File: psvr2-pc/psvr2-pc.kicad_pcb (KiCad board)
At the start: 2 copper layers, 5 parts, among them Q1 IRLML6244, U1 RP2040, U2 M95256-WMN6P, U3 FUSB302B01MPX, U4 FUSB302B01MPX

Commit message: Mess around with KiBuzzard and the PCB Editor.
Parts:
- added kibuzzard-65BD64CF: G***, kibuzzard-65BD64CF, F.Cu at (63.5, 22.9)
- moved U3 89.8 mm to (126.2, 26.7)
- moved U4 32.1 mm to (67.3, 50.3)
- moved U1 29.1 mm to (58.4, 37.2)
- moved U2 10.3 mm to (20.3, 38.7)
- moved Q1 4.74 mm to (42.2, 24.4)

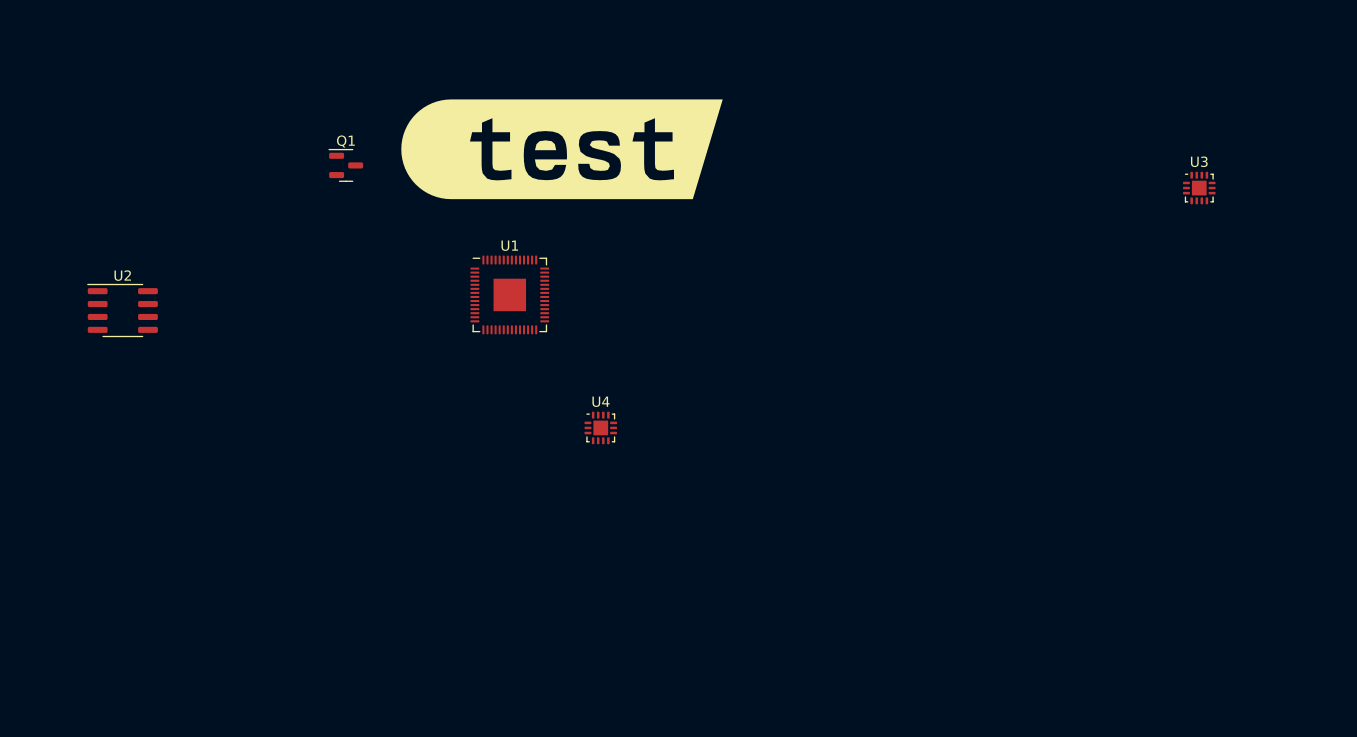
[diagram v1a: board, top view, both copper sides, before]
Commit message: Start documenting the valid half-duplex M-LVDS transceivers >1Mbps that work for converting the differential DP-AUX signals into something that the microcontroller GPIO can understand.
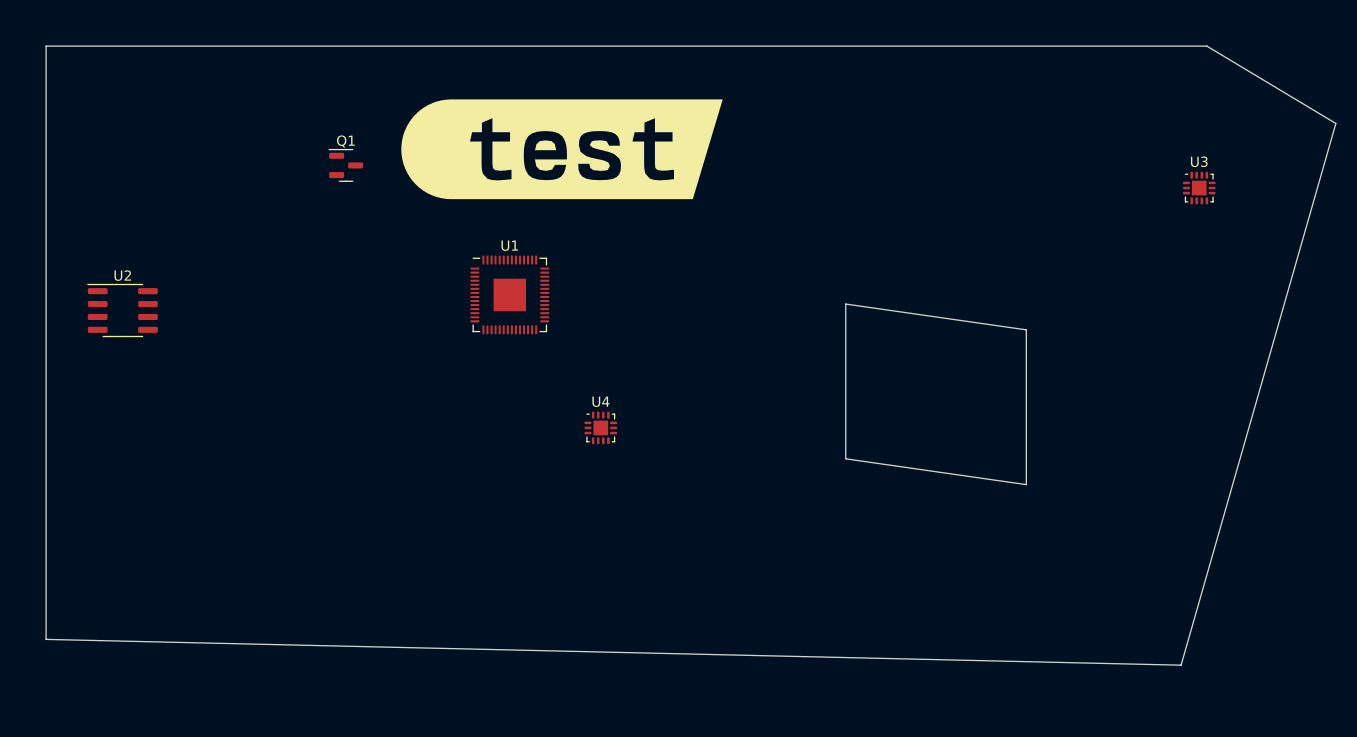
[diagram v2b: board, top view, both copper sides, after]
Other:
- board outline added: 127 x 61 mm
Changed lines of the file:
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@@
     (attr board_only exclude_from_pos_files exclude_from_bom)
     (fp_text reference "kibuzzard-65BD64CF" (at 0 -7.958243) (layer "F.SilkS") hide
-        (effects (font (size 0 0)))
+        (effects (font (size 0 0) (thickness 0.15)))
     )
     (fp_text value "G***" (at 0 7.958243) (layer "F.SilkS") hide
-        (effects (font (size 0 0)))
+        (effects (font (size 0 0) (thickness 0.15)))
     )
     (fp_poly
@@
       (stroke (width 0) (type solid)) (fill solid) (layer "F.SilkS"))
   )
+  (gr_line (start 109.22 55.88) (end 109.22 40.64)
+    (stroke (width 0.1) (type default)) (layer "Edge.Cuts"))
+  (gr_line (start 91.44 38.1) (end 91.44 53.34)
+    (stroke (width 0.1) (type default)) (layer "Edge.Cuts"))
+  (gr_line (start 139.7 20.32) (end 127 12.7)
+    (stroke (width 0.1) (type default)) (layer "Edge.Cuts"))
+  (gr_line (start 109.22 40.64) (end 91.44 38.1)
+    (stroke (width 0.1) (type default)) (layer "Edge.Cuts"))
+  (gr_line (start 124.46 73.66) (end 139.7 20.32)
+    (stroke (width 0.1) (type default)) (layer "Edge.Cuts"))
+  (gr_line (start 12.7 12.7) (end 12.7 71.12)
+    (stroke (width 0.1) (type default)) (layer "Edge.Cuts"))
+  (gr_line (start 127 12.7) (end 12.7 12.7)
+    (stroke (width 0.1) (type default)) (layer "Edge.Cuts"))
+  (gr_line (start 12.7 71.12) (end 124.46 73.66)
+    (stroke (width 0.1) (type default)) (layer "Edge.Cuts"))
+  (gr_line (start 91.44 53.34) (end 109.22 55.88)
+    (stroke (width 0.1) (type default)) (layer "Edge.Cuts"))
 )

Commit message: Mark the power and config DisplayPort pins as not connected.
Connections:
- U1 pad 2: unconnected-(U1-GPIO0-Pad2) -> /HMD_TYC_SDA
- U1 pad 3: unconnected-(U1-GPIO1-Pad3) -> /HMD_TYC_SCL
- U1 pad 4: unconnected-(U1-GPIO2-Pad4) -> /HMD_TYC_INT
- U1 pad 46: unconnected-(U1-USB_DM-Pad46) -> /PC_USB2.0_P
- U1 pad 47: unconnected-(U1-USB_DP-Pad47) -> /PC_USB2.0_N
- U1 pad 57: unconnected-(U1-GND-Pad57) -> GND
- U3 pad 2: unconnected-(U3-VBUS-Pad2) -> Net-(U3-VBUS)
- U3 pad 5: unconnected-(U3-INT_N-Pad5) -> /HMD_TYC_INT
- U3 pad 6: unconnected-(U3-SCL-Pad6) -> /HMD_TYC_SCL
- U3 pad 7: unconnected-(U3-SDA-Pad7) -> /HMD_TYC_SDA
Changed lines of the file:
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@@
   (net 3 "unconnected-(Q1-D-Pad3)")
   (net 4 "Net-(U1-IOVDD-Pad1)")
-  (net 5 "unconnected-(U1-GPIO0-Pad2)")
-  (net 6 "unconnected-(U1-GPIO1-Pad3)")
-  (net 7 "unconnected-(U1-GPIO2-Pad4)")
+  (net 5 "/HMD_TYC_SDA")
+  (net 6 "/HMD_TYC_SCL")
+  (net 7 "/HMD_TYC_INT")
   (net 8 "unconnected-(U1-GPIO3-Pad5)")
   (net 9 "unconnected-(U1-GPIO4-Pad6)")
@@
   (net 59 "unconnected-(U2-VCC-Pad8)")
   (net 60 "Net-(U3-VDD-Pad3)")
-  (net 61 "unconnected-(U3-INT_N-Pad5)")
-  (net 62 "unconnected-(U3-SCL-Pad6)")
-  (net 63 "unconnected-(U3-SDA-Pad7)")
+  (net 61 "/PC_USB2.0_P")
+  (net 62 "/PC_USB2.0_N")
+  (net 63 "GND")
   (net 64 "Net-(U3-GND-Pad15)")
   (net 65 "unconnected-(U3-VCONN-Pad12)")
@@
   (net 74 "unconnected-(U4-VCONN-Pad12)")
   (net 75 "unconnected-(U4-VCONN-Pad13)")
-  (net 76 "unconnected-(U3-VBUS-Pad2)")
-  (net 77 "unconnected-(U1-USB_DP-Pad47)")
-  (net 78 "unconnected-(U1-USB_DM-Pad46)")
-  (net 79 "unconnected-(U1-GND-Pad57)")
-  (net 80 "Net-(U4-CC2-Pad1)")
-  (net 81 "Net-(U3-CC2-Pad1)")
-  (net 82 "Net-(U3-CC1-Pad10)")
+  (net 76 "Net-(P1-VCONN)")
+  (net 77 "Net-(U3-VBUS)")
+  (net 78 "Net-(P1-CC)")
+  (net 79 "Net-(D2-K)")
   (footprint "Package_DFN_QFN:QFN-56-1EP_7x7mm_P0.4mm_EP3.2x3.2mm" (layer "F.Cu")
     (at 58.36 37.2025)
@@
       (net 4 "Net-(U1-IOVDD-Pad1)") (pinfunction "IOVDD") (pintype "power_in"))
     (pad "2" smd roundrect (at -3.4375 -2.2) (size 0.875 0.2) (layers "F.Cu" "F.Paste" "F.Mask") (roundrect_rratio 0.25)
-      (net 5 "unconnected-(U1-GPIO0-Pad2)") (pinfunction "GPIO0") (pintype "bidirectional"))
+      (net 5 "/HMD_TYC_SDA") (pinfunction "GPIO0") (pintype "bidirectional"))
     (pad "3" smd roundrect (at -3.4375 -1.8) (size 0.875 0.2) (layers "F.Cu" "F.Paste" "F.Mask") (roundrect_rratio 0.25)
-      (net 6 "unconnected-(U1-GPIO1-Pad3)") (pinfunction "GPIO1") (pintype "bidirectional"))
+      (net 6 "/HMD_TYC_SCL") (pinfunction "GPIO1") (pintype "bidirectional"))
     (pad "4" smd roundrect (at -3.4375 -1.4) (size 0.875 0.2) (layers "F.Cu" "F.Paste" "F.Mask") (roundrect_rratio 0.25)
-      (net 7 "unconnected-(U1-GPIO2-Pad4)") (pinfunction "GPIO2") (pintype "bidirectional"))
+      (net 7 "/HMD_TYC_INT") (pinfunction "GPIO2") (pintype "bidirectional"))
     (pad "5" smd roundrect (at -3.4375 -1) (size 0.875 0.2) (layers "F.Cu" "F.Paste" "F.Mask") (roundrect_rratio 0.25)
       (net 8 "unconnected-(U1-GPIO3-Pad5)") (pinfunction "GPIO3") (pintype "bidirectional"))
@@
       (net 44 "unconnected-(U1-VREG_VOUT-Pad45)") (pinfunction "VREG_VOUT") (pintype "power_out"))
     (pad "46" smd roundrect (at 1.4 -3.4375) (size 0.2 0.875) (layers "F.Cu" "F.Paste" "F.Mask") (roundrect_rratio 0.25)
-      (net 78 "unconnected-(U1-USB_DM-Pad46)") (pinfunction "USB_DM") (pintype "bidirectional"))
+      (net 61 "/PC_USB2.0_P") (pinfunction "USB_DM") (pintype "bidirectional"))
     (pad "47" smd roundrect (at 1 -3.4375) (size 0.2 0.875) (layers "F.Cu" "F.Paste" "F.Mask") (roundrect_rratio 0.25)
-      (net 77 "unconnected-(U1-USB_DP-Pad47)") (pinfunction "USB_DP") (pintype "bidirectional"))
+      (net 62 "/PC_USB2.0_N") (pinfunction "USB_DP") (pintype "bidirectional"))
     (pad "48" smd roundrect (at 0.6 -3.4375) (size 0.2 0.875) (layers "F.Cu" "F.Paste" "F.Mask") (roundrect_rratio 0.25)
       (net 45 "unconnected-(U1-USB_VDD-Pad48)") (pinfunction "USB_VDD") (pintype "power_in"))
@@
       (net 51 "unconnected-(U1-QSPI_SS-Pad56)") (pinfunction "QSPI_SS") (pintype "bidirectional"))
     (pad "57" smd rect (at 0 0) (size 3.2 3.2) (layers "F.Cu" "F.Mask")
-      (net 79 "unconnected-(U1-GND-Pad57)") (pinfunction "GND") (pintype "power_in"))
+      (net 63 "GND") (pinfunction "GND") (pintype "power_in"))
     (model "${KICAD6_3DMODEL_DIR}/Package_DFN_QFN.3dshapes/QFN-56-1EP_7x7mm_P0.4mm_EP3.2x3.2mm.wrl"
       (offset (xyz 0 0 0))
@@
     (pad "" smd roundrect (at 0.36 0.36) (size 0.58 0.58) (layers "F.Paste") (roundrect_rratio 0.25))
     (pad "1" smd roundrect (at -1.2625 -0.5) (size 0.675 0.25) (layers "F.Cu" "F.Paste" "F.Mask") (roundrect_rratio 0.25)
-      (net 80 "Net-(U4-CC2-Pad1)") (pinfunction "CC2") (pintype "bidirectional"))
+      (net 67 "Net-(J4-CC2)") (pinfunction "CC2") (pintype "bidirectional"))
     (pad "2" smd roundrect (at -1.2625 0) (size 0.675 0.25) (layers "F.Cu" "F.Paste" "F.Mask") (roundrect_rratio 0.25)
-      (net 67 "Net-(J4-CC2)") (pinfunction "VBUS") (pintype "input"))
+      (net 79 "Net-(D2-K)") (pinfunction "VBUS") (pintype "input"))
     (pad "3" smd roundrect (at -1.2625 0.5) (size 0.675 0.25) (layers "F.Cu" "F.Paste" "F.Mask") (roundrect_rratio 0.25)
       (net 68 "Net-(U4-VDD-Pad3)") (pinfunction "VDD") (pintype "power_in"))
@@
       (net 75 "unconnected-(U4-VCONN-Pad13)") (pinfunction "VCONN") (pintype "power_in"))
     (pad "14" smd roundrect (at -0.75 -1.2625) (size 0.25 0.675) (layers "F.Cu" "F.Paste" "F.Mask") (roundrect_rratio 0.25)
-      (net 80 "Net-(U4-CC2-Pad1)") (pinfunction "CC2") (pintype "bidirectional"))
+      (net 67 "Net-(J4-CC2)") (pinfunction "CC2") (pintype "bidirectional"))
     (pad "15" smd rect (at 0 0) (size 1.45 1.45) (layers "F.Cu" "F.Mask")
       (net 72 "Net-(U4-GND-Pad15)") (pinfunction "GND") (pintype "passive"))
@@
     (pad "" smd roundrect (at 0.36 0.36) (size 0.58 0.58) (layers "F.Paste") (roundrect_rratio 0.25))
     (pad "1" smd roundrect (at -1.2625 -0.5) (size 0.675 0.25) (layers "F.Cu" "F.Paste" "F.Mask") (roundrect_rratio 0.25)
-      (net 81 "Net-(U3-CC2-Pad1)") (pinfunction "CC2") (pintype "bidirectional"))
+      (net 76 "Net-(P1-VCONN)") (pinfunction "CC2") (pintype "bidirectional"))
     (pad "2" smd roundrect (at -1.2625 0) (size 0.675 0.25) (layers "F.Cu" "F.Paste" "F.Mask") (roundrect_rratio 0.25)
-      (net 76 "unconnected-(U3-VBUS-Pad2)") (pinfunction "VBUS") (pintype "input"))
+      (net 77 "Net-(U3-VBUS)") (pinfunction "VBUS") (pintype "input"))
     (pad "3" smd roundrect (at -1.2625 0.5) (size 0.675 0.25) (layers "F.Cu" "F.Paste" "F.Mask") (roundrect_rratio 0.25)
       (net 60 "Net-(U3-VDD-Pad3)") (pinfunction "VDD") (pintype "power_in"))
@@
       (net 60 "Net-(U3-VDD-Pad3)") (pinfunction "VDD") (pintype "passive"))
     (pad "5" smd roundrect (at -0.25 1.2625) (size 0.25 0.675) (layers "F.Cu" "F.Paste" "F.Mask") (roundrect_rratio 0.25)
-      (net 61 "unconnected-(U3-INT_N-Pad5)") (pinfunction "INT_N") (pintype "open_collector"))
+      (net 7 "/HMD_TYC_INT") (pinfunction "INT_N") (pintype "open_collector"))
     (pad "6" smd roundrect (at 0.25 1.2625) (size 0.25 0.675) (layers "F.Cu" "F.Paste" "F.Mask") (roundrect_rratio 0.25)
-      (net 62 "unconnected-(U3-SCL-Pad6)") (pinfunction "SCL") (pintype "input"))
+      (net 6 "/HMD_TYC_SCL") (pinfunction "SCL") (pintype "input"))
     (pad "7" smd roundrect (at 0.75 1.2625) (size 0.25 0.675) (layers "F.Cu" "F.Paste" "F.Mask") (roundrect_rratio 0.25)
-      (net 63 "unconnected-(U3-SDA-Pad7)") (pinfunction "SDA") (pintype "bidirectional"))
+      (net 5 "/HMD_TYC_SDA") (pinfunction "SDA") (pintype "bidirectional"))
     (pad "8" smd roundrect (at 1.2625 0.5) (size 0.675 0.25) (layers "F.Cu" "F.Paste" "F.Mask") (roundrect_rratio 0.25)
       (net 64 "Net-(U3-GND-Pad15)") (pinfunction "GND") (pintype "power_in"))
@@
       (net 64 "Net-(U3-GND-Pad15)") (pinfunction "GND") (pintype "passive"))
     (pad "10" smd roundrect (at 1.2625 -0.5) (size 0.675 0.25) (layers "F.Cu" "F.Paste" "F.Mask") (roundrect_rratio 0.25)
-      (net 82 "Net-(U3-CC1-Pad10)") (pinfunction "CC1") (pintype "bidirectional"))
+      (net 78 "Net-(P1-CC)") (pinfunction "CC1") (pintype "bidirectional"))
     (pad "11" smd roundrect (at 0.75 -1.2625) (size 0.25 0.675) (layers "F.Cu" "F.Paste" "F.Mask") (roundrect_rratio 0.25)
-      (net 82 "Net-(U3-CC1-Pad10)") (pinfunction "CC1") (pintype "bidirectional"))
+      (net 78 "Net-(P1-CC)") (pinfunction "CC1") (pintype "bidirectional"))
     (pad "12" smd roundrect (at 0.25 -1.2625) (size 0.25 0.675) (layers "F.Cu" "F.Paste" "F.Mask") (roundrect_rratio 0.25)
       (net 65 "unconnected-(U3-VCONN-Pad12)") (pinfunction "VCONN") (pintype "power_in"))
@@
       (net 66 "unconnected-(U3-VCONN-Pad13)") (pinfunction "VCONN") (pintype "power_in"))
     (pad "14" smd roundrect (at -0.75 -1.2625) (size 0.25 0.675) (layers "F.Cu" "F.Paste" "F.Mask") (roundrect_rratio 0.25)
-      (net 81 "Net-(U3-CC2-Pad1)") (pinfunction "CC2") (pintype "bidirectional"))
+      (net 76 "Net-(P1-VCONN)") (pinfunction "CC2") (pintype "bidirectional"))
     (pad "15" smd rect (at 0 0) (size 1.45 1.45) (layers "F.Cu" "F.Mask")
       (net 64 "Net-(U3-GND-Pad15)") (pinfunction "GND") (pintype "passive"))

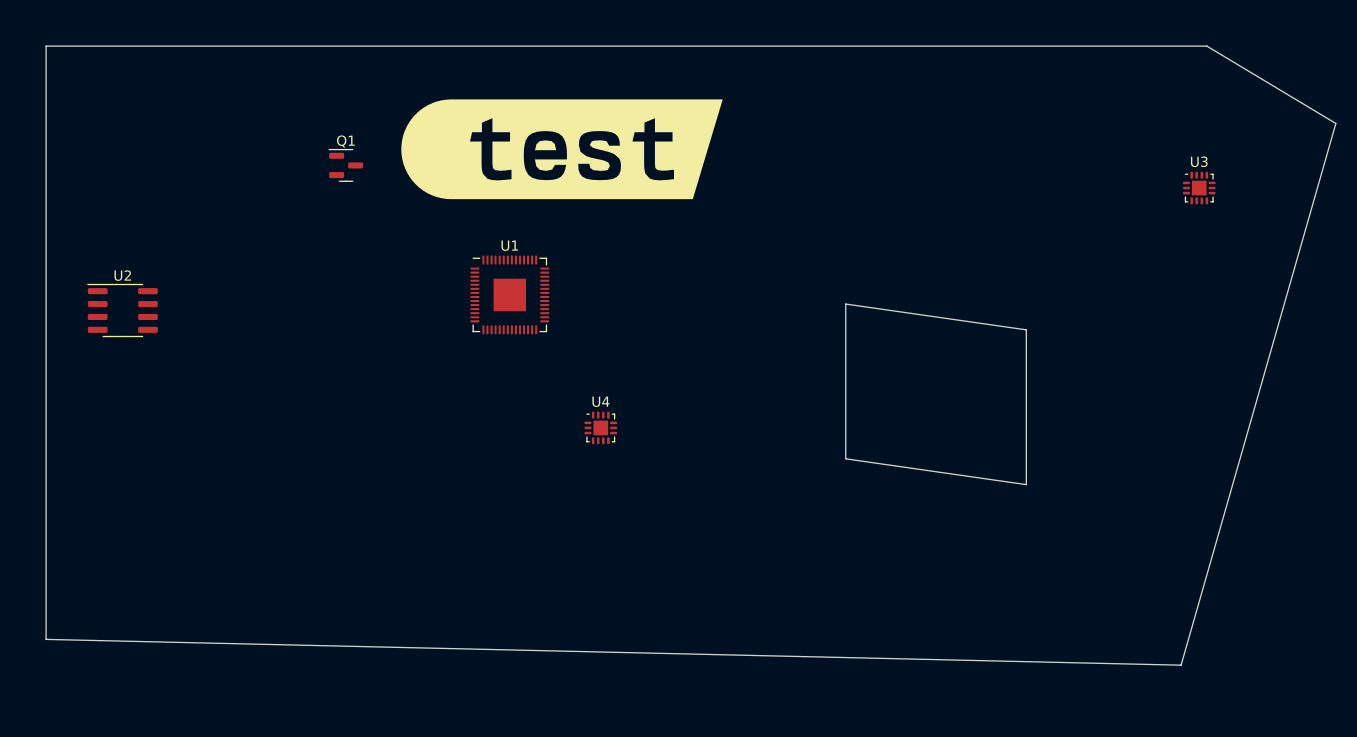
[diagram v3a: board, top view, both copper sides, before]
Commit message: Mess around with the footprint downloader, can't seem to get 3D models out of anything that I can actually pick from the Chinese site. ¯\_(ツ)_/¯
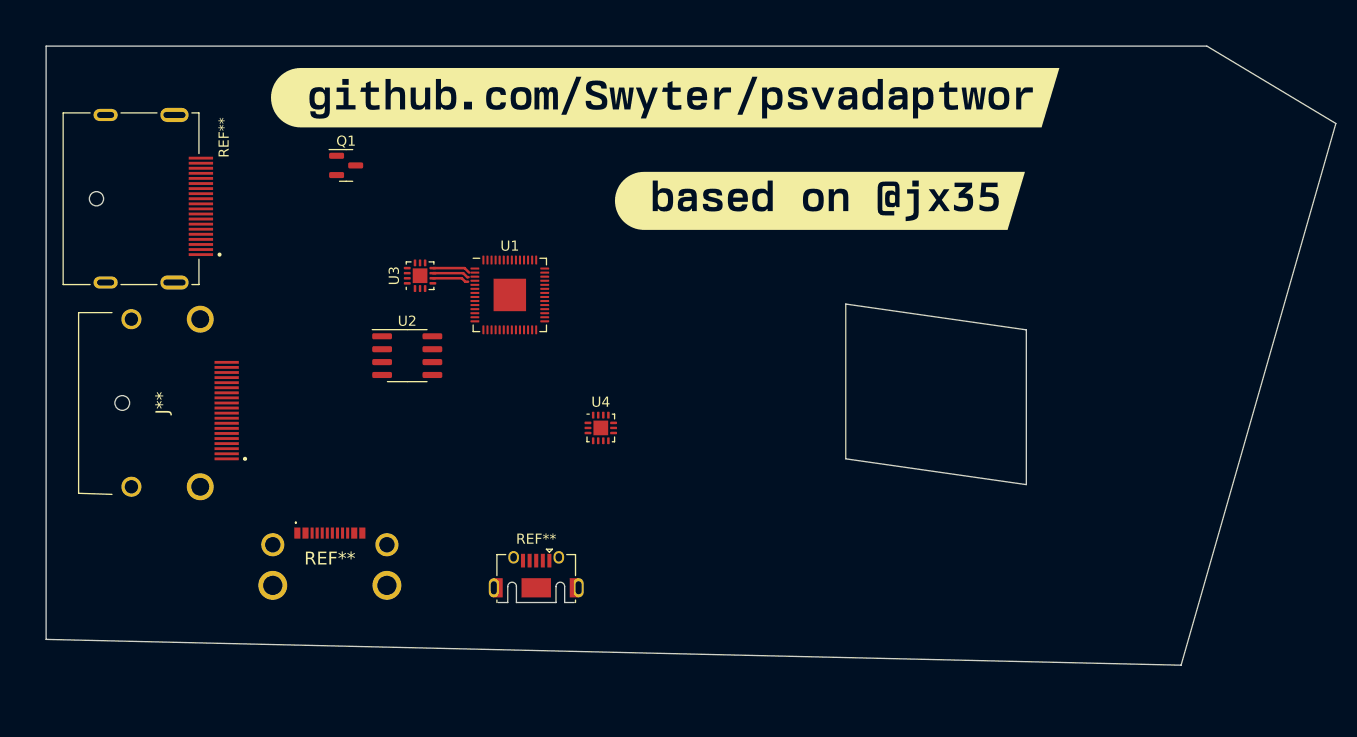
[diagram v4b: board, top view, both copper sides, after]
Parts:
- removed kibuzzard-65BD64CF: G***, kibuzzard-65BD64CF
- added J**: 472720001, Samacsys:472720001, F.Cu at (23.2, 47.8)
- added REF**: 2169900002, Samacsys:2169900002, F.Cu at (40.6, 63.5)
- added REF**: USB_Micro-AB_Molex_47590-0001, Connector_USB:USB_Micro-AB_Molex_47590-0001, F.Cu at (61.0, 66.0)
- added REF**: MOLEX_47272-0001, Snapeda:47272-0001_MOLEX_47272-0001, F.Cu at (14.4, 27.7)
- added kibuzzard-65BF205B: G***, kibuzzard-65BF205B, F.Cu at (88.9, 27.9)
- added kibuzzard-65BF20B5: G***, kibuzzard-65BF20B5, F.Cu at (73.7, 17.8)
- moved U3 77.2 mm to (49.5, 35.3), turned to 90 degrees
- moved U2 28.4 mm to (48.3, 43.2)
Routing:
- net /HMD_TYC_SDA: track 0.00 -> 3.75 mm
- net /HMD_TYC_SCL: track 0.00 -> 3.68 mm
- net /HMD_TYC_INT: track 0.00 -> 3.61 mm

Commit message: Start adding the missing footprints to the schematic and editing/assigning broken 3D models, play around with PCB placement.
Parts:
- added D1: BAT54GWJ, Diode_SMD:D_SOD-110, F.Cu at (137.0, 72.0)
- added D2: BAT54GWJ, Diode_SMD:D_SOD-123, F.Cu at (66.0, 56.0)
- added J2: USB3_B_Micro, Samacsys:2169900002, F.Cu at (130.0, 63.0)
- added J3: DP_47272, Samacsys:472720001, F.Cu at (86.0, 45.0)
- added J4: USB_C_Receptacle_USB2.0_14P, Samacsys:2169900002, F.Cu at (84.0, 59.0)
- added P1: USB_C_Plug, Samacsys:2169900002, F.Cu at (51.0, 53.0)
- added Y1: Crystal, Oscillator:Oscillator_SMD_Abracon_ASCO-4Pin_1.6x1.2mm, F.Cu at (58.0, 45.0)
